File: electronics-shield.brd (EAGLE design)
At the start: 64.9 x 56 mm, 92 parts, among them IC1 TLE9201SG, IC2 TLE9201SG, IC3 TLE9201SG, IC4 TLE9201SG, IC5 AOZ1232QI-01, IC6 AOZ1232QI-01, IC7 DS3231SN#, J1 USB-MICRO-B, Q2 ON-SEMICONDUCTOR---NTZD3154NT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, Q3 ON-SEMICONDUCTOR---NTZD3154NT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, U1 STM32F0XX8T, U2 EEPROM-I2C, X1 CONNECTOR_PHOENIX_3.81, X2 Listwa zaciskowa rozłączalna 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, Y2 8MHz

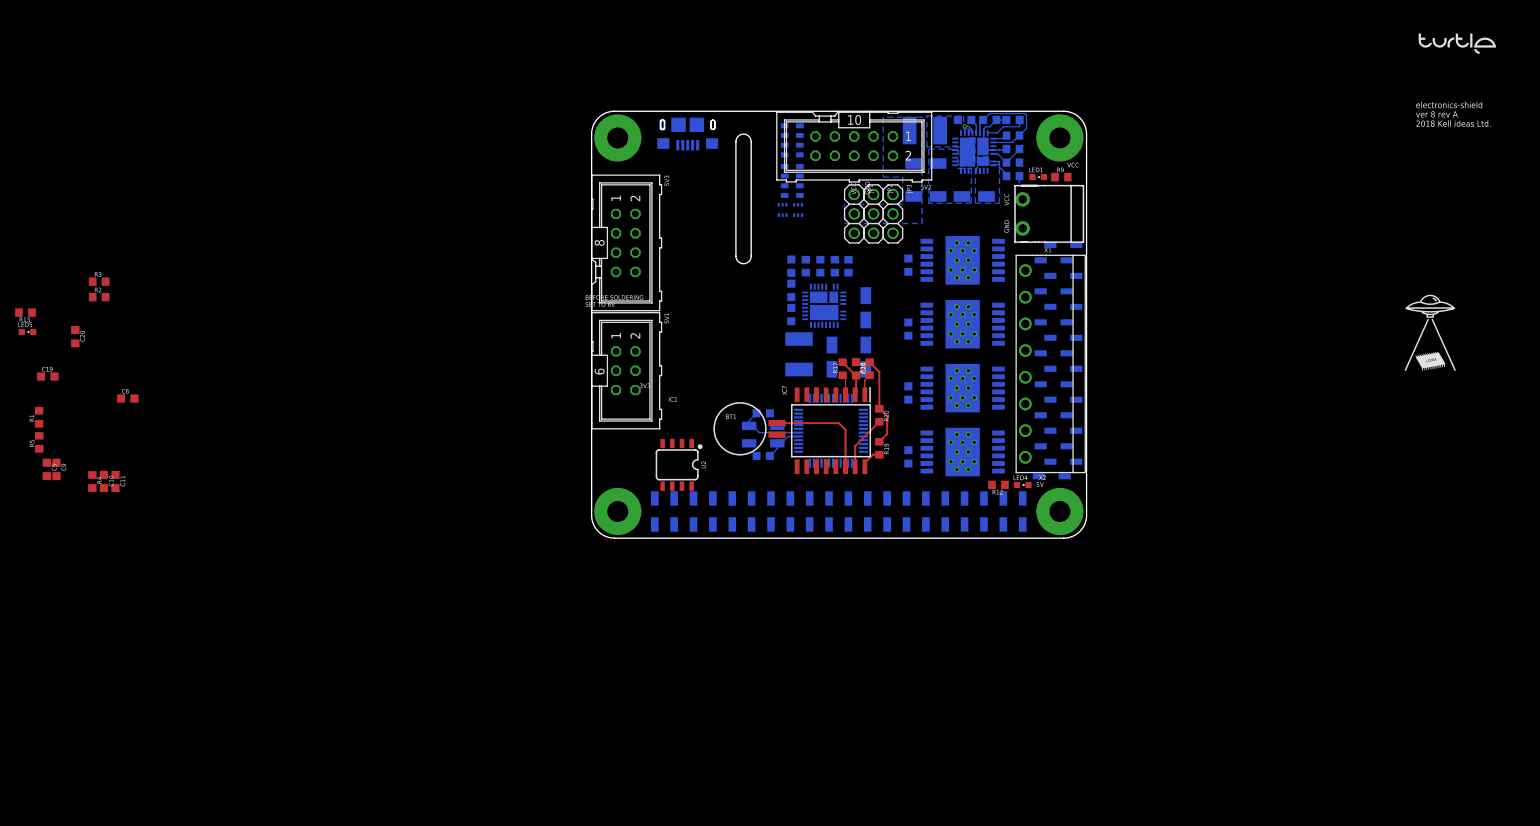
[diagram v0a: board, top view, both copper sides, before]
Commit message: Merge branch 'add_RTC' into development
First, basic layout
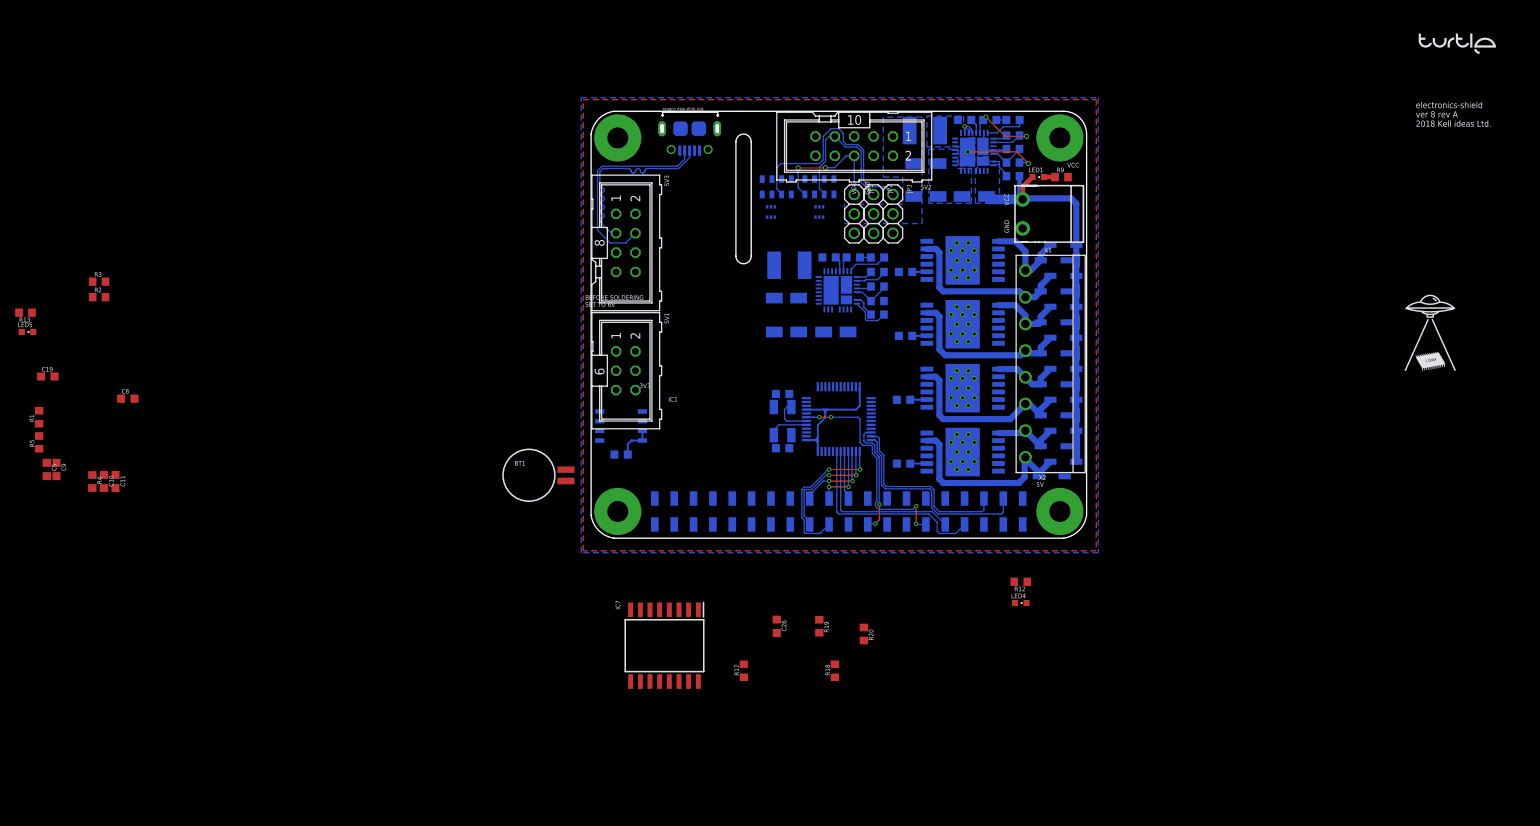
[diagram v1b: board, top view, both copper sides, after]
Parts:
- removed J1: USB-MICRO-B, Kell Ideas:USB-MICRO-B
- added USB1: ZX62-B-5PA, Seeed-Connector:MICRO-USB5+6P-SMD-0.65-AB
- moved C20 73.3 mm to (3.71, 11.1), flipped to the bottom, turned to 0 degrees
- moved R17 41.7 mm to (19.8, -17.3)
- moved R18 39.9 mm to (31.8, -17.3)
- moved IC7 35.7 mm to (9.40, -14.0)
- moved C26 35.4 mm to (24.1, -11.4)
- moved R20 28.8 mm to (35.6, -12.4)
- moved BT1 28.3 mm to (-8.38, 8.38)
- moved R19 24.7 mm to (29.7, -11.4)
- moved LED4 15.5 mm to (56.1, -8.38)
- moved R12 13.0 mm to (56.1, -5.59)
- moved L2 11.8 mm to (25.8, 35.9), turned to 0 degrees
- moved C24 11.4 mm to (37.3, 37.0), turned to 180 degrees
- moved C21 10.9 mm to (25.4, 27.2), turned to 0 degrees
- moved C22 9.78 mm to (25.4, 31.6), turned to 0 degrees
- moved R15 9.43 mm to (37.3, 35.1), turned to 0 degrees
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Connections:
- net DATA_N: now also USB1.3; no longer J1.D-
- net DATA_P: now also USB1.2; no longer J1.D+
- net GND: now also USB1.5, USB1.P1, USB1.P2, USB1.P3, USB1.P4, USB1.P5, USB1.P6; no longer J1.GND, J1.SHIELD$1, J1.SHIELD$2, J1.SHIELD$3, J1.SHIELD$4
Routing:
- net VCC: track 0.93 -> 58.6 mm
- net SERVO3: track 0.00 -> 29.8 mm
- net NRST: track 0.00 -> 29.5 mm, vias 0 -> 4
- net DATA_P: track 0.00 -> 27.2 mm
- net RPI_TXD: track 0.00 -> 27.0 mm
- net MOT41: track 0.00 -> 26.5 mm
- net DATA_N: track 0.00 -> 26.2 mm
- net MOT31: track 0.00 -> 23.9 mm
- net MOT11: track 0.00 -> 23.1 mm
- net MOT21: track 0.00 -> 22.7 mm
- net RPI_RXD: track 0.00 -> 22.2 mm
- net SCL: track 2.86 -> 24.9 mm
- net SWCLK: track 0.00 -> 20.7 mm, vias 0 -> 2
- net SDA: track 7.21 -> 27.5 mm
- net SERVO2: track 0.00 -> 19.8 mm
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- added copper zone on layer 1, net GND
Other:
- board size 64.9 x 56 mm -> 65 x 56 mm

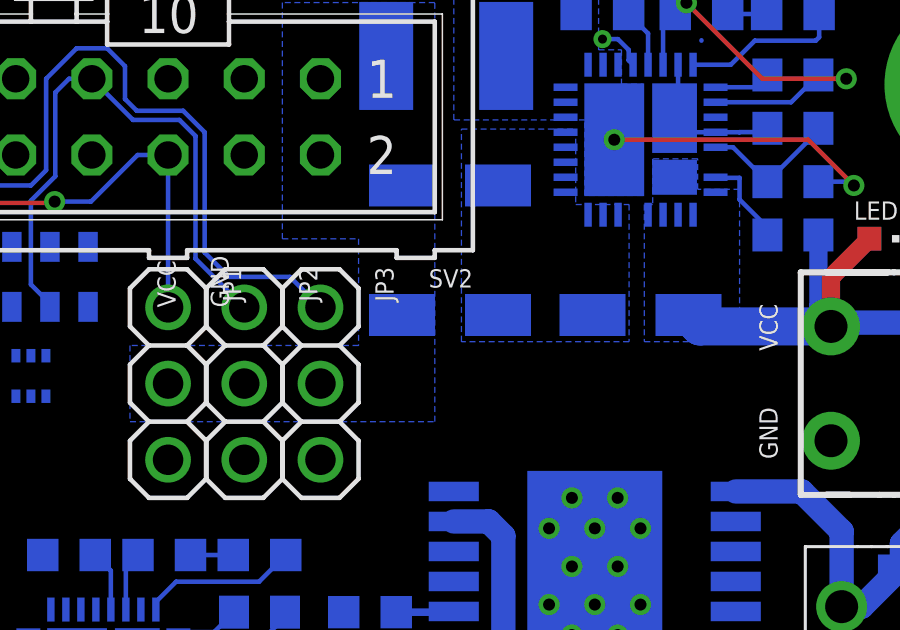
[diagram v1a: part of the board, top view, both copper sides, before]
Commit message: Added values for parts in dc-dc converter
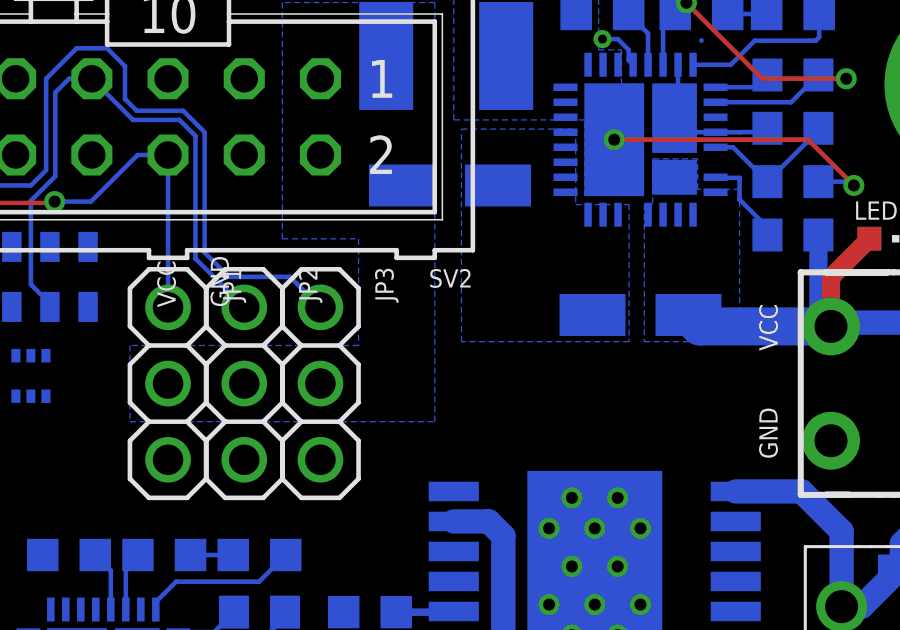
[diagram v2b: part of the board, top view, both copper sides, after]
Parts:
- removed C13: (no value), rcl:PANASONIC_B
- C12: value (none) -> 22uF
- C14: value (none) -> 100uF
- C15: value (none) -> 100n
- C16: value (none) -> 1uf
- C17: value (none) -> 1nF
- L1, L2: value (none) -> 100uH
- R6: value (none) -> 65k
- R7: value (none) -> 10k
- R8: value (none) -> 100k
- renumbered R10 to 456
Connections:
- net GND: no longer C13.-
- net VCC_SERVO: no longer C13.+

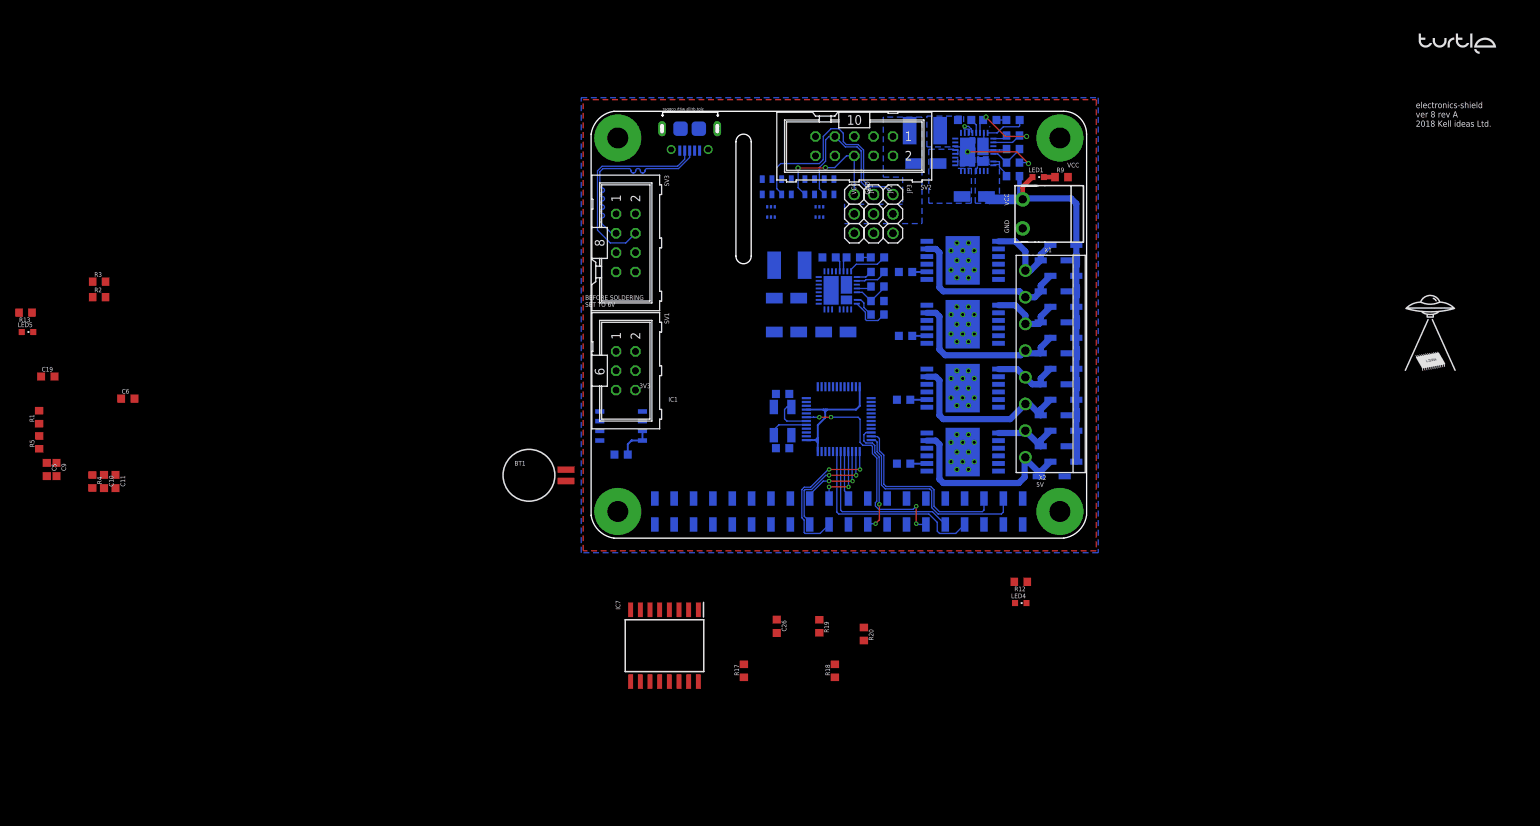
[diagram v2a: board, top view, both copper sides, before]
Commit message: Minor changes, changed RTC, added 3V3 regulator, changed USB connector, added fuses, reverse polarity protection, changed footprint for Schottky diodes, added filtering to input voltage, change in layout
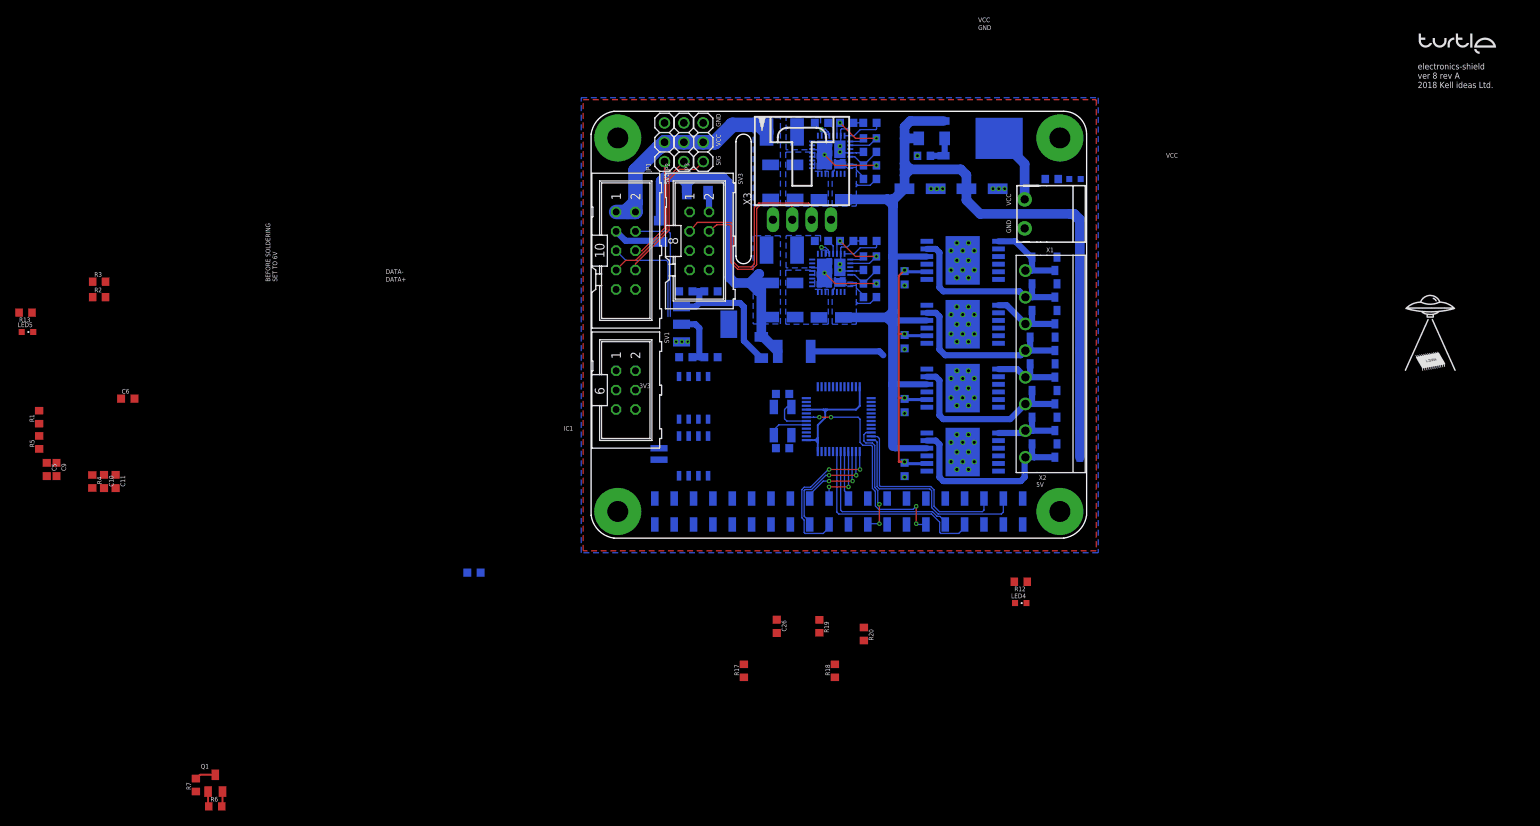
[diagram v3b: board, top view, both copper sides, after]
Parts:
- removed 456: (no value), Kell Ideas:R0603
- removed C19: (no value), Kell Ideas:C0603K
- removed IC5: AOZ1232QI-01, Kell Ideas:AOZ1232QI01
- removed IC7: DS3231SN#, Kell Ideas:SOIC127P1032X265-16N
- removed L1: 100uH, rcl:L4532P
- removed Q3: ON-SEMICONDUCTOR---NTZD3154NT1G_ON_SEMICONDUCTOR_NTZD3154NT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, electronics-shield:ON-SEMICONDUCTOR---NTZD3154NT1G_ON_SEMICONDUCTOR_NTZD3154NT1G_0
- removed RN1, RN2: 1k, SparkFun-Resistors:0805-ARV
- removed USB1: ZX62-B-5PA, Seeed-Connector:MICRO-USB5+6P-SMD-0.65-AB
- added C13: 47uF, rcl:PANASONIC_C
- added C27, C31, C32: 33uF/10V, rcl:PANASONIC_B
- added C28: 100n, Kell Ideas:C0603K
- added C29: 1nF, Kell Ideas:C0603K
- added C30: 1uF/35V, Kell Ideas:C0603K
- added D17: 10V, diode:SOD80C
- added F1, F2, F5: 750mA, Seeed-Fuse:F1206
- added F3: MF-MSMF050-2, Seeed-Fuse:F1812
- added IC8: AOZ1232QI-01, Kell Ideas:AOZ1232QI01
- added L3: 1uH, rcl:L4532P
- added Q1: (no value), adafruit:SOT23
- added R21: 10k, Kell Ideas:R0603
- added R22: 100k, Kell Ideas:R0603
- added R23, R24: 456, Kell Ideas:R0603
- added U3: MAXIM_DS3231MZ+MAXIM_DS3231MZ+_0_0, Kell Ideas:MAXIM_DS3231MZ+_0
- added U4: V_REG_317SMD, Kell Ideas:SOT223
- added X3: C-GRID-04-70553, con-molex:70553-04
- C1, C2, C3, C4: value (none) -> 100nF
- C12: value 22uF -> 47uF; device rcl:PANASONIC_B -> rcl:PANASONIC_C
- C14: value 100uF -> 22uF; device rcl:PANASONIC_B -> Kell Ideas:C0603K
- C15: value 100n -> 100nF
- C16: value 1uf -> 100nF
- C17: value 1nF -> 22uF
- C18: value (none) -> 22uF/35V
- C21: value (none) -> 33uF/10V
- C22: value (none) -> 100n; device rcl:PANASONIC_B -> Kell Ideas:C0603K
- C23: value (none) -> 1nF
- C24: value (none) -> 1uF/35V
- C25: value (none) -> 22uF/35V; device Kell Ideas:C0603K -> rcl:PANASONIC_B
- D1, D10, D11, D12, D13, D14, D15, D16, D2, D3, D4, D5, D6, D7, D8, D9: value SK38SMA -> 80V/3A; device Kell Ideas:SOD123 -> adafruit:SOD-123FL
- L2: value 100uH -> 1uH
- Q2: value ON-SEMICONDUCTOR---NTZD3154NT1G_ON_SEMICONDUCTOR_NTZD3154NT1GON_SEMICONDUCTOR_NTZD3154NT1G_0_0 -> IRFR5305; device electronics-shield:ON-SEMICONDUCTOR---NTZD3154NT1G_ON_SEMICONDUCTOR_NTZD3154NT1G_0 -> transistor-power:D-PAK_TO252AA
- R11, R16: value (none) -> 65k
- R14: value (none) -> 10k
- R15: value (none) -> 100k
- R6: value 65k -> 10k; device Kell Ideas:R0603 -> rcl:R0603
- R7: device Kell Ideas:R0603 -> rcl:R0603
- R8: value 100k -> 10k; device Kell Ideas:R0603 -> rcl:R0603
- moved R7 135.8 mm to (-52.1, -32.3), flipped to the top, turned to 90 degrees
- moved R6 134.5 mm to (-49.5, -35.1), flipped to the top
- moved C17 50.4 mm to (15.5, 23.9), turned to 0 degrees
- moved C15 42.9 mm to (12.2, 32.5)
- moved C16 42.9 mm to (15.5, 32.5)
- moved C14 40.5 mm to (12.2, 23.9), turned to 180 degrees
- moved SV2 33.0 mm to (4.32, 37.8), turned to 270 degrees
- moved Q2 29.1 mm to (50.8, 52.6)
- moved JP1 26.6 mm to (9.40, 52.1), turned to 90 degrees
- moved JP2 26.6 mm to (11.9, 52.1), turned to 90 degrees
- moved JP3 26.6 mm to (14.5, 52.1), turned to 90 degrees
- moved C20 24.8 mm to (-15.6, -4.39)
- moved C22 23.4 mm to (30.0, 54.6), turned to 180 degrees
- moved C21 21.9 mm to (24.9, 49.1)
- moved C23 18.5 mm to (36.3, 54.6)
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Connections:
- removed net +5V/2: SV2.3
- removed net BST: C15.2, IC5.27
- removed net FB: IC5.5, R6.2, R7.1
- removed net LX: C15.1, IC5.20, IC5.21, IC5.22, IC5.23, IC5.24, IC5.25, IC5.31, L1.1, R6.1
- removed net LX1: C23.1, IC6.20, IC6.21, IC6.22, IC6.23, IC6.24, IC6.25, IC6.31, L2.1, R11.1
- removed net N$14: Q2.4, RN2.3
- removed net N$16: Q2.3, RN2.4
- removed net PGOOD: IC5.1, R8.2
- removed net SEN1: U1.10
- removed net SEN2: U1.11
- removed net SEN3: U1.12
- removed net SEN4: U1.13
- removed net SS: C17.2, IC5.30
- removed net TON: 456.2, IC5.6
- removed net VCC_INT: C16.2, IC5.2, IC5.28, R8.1
- new net BST2: C28.2, IC8.27
- new net FB2: IC8.5, R16.2, R21.1
- new net LX2: C28.1, IC8.20, IC8.21, IC8.22, IC8.23, IC8.24, IC8.25, IC8.31, L3.1, R16.1
- new net LX3: C22.1, IC6.20, IC6.21, IC6.22, IC6.23, IC6.24, IC6.25, IC6.31, L2.1, R11.1
- new net N$12: F2.2, SV2.3
- new net N$13: D17.A, Q2.1, R8.2
- new net N$15: F1.1, SV3.2
- new net N$17: C15.2, C16.2, F5.2, U4.3
- new net N$18: F3.1, PCB1.2, PCB1.4
- new net PGOOD2: IC8.1, R22.2
- new net SS2: C29.2, IC8.30
- new net TON2: IC8.6, R23.2
- new net UART_SELECTOR: PCB1.7
- new net V+: Q2.4, X1.2
- new net VBAT: U3.6
- new net VCC_INT2: C30.2, IC8.2, IC8.28, R22.1
- net +3V3: now also C14.2, C17.2, Q1.1, R6.1, U4.2; no longer IC7.2, Q2.2, Q2.5, Q3.2, Q3.5, RN1.6, RN1.8, RN2.6, RN2.8
- net +5V: now also C27.+, C31.+, F1.2, F2.1, F3.2, F5.1, L3.2, R7.1; no longer C19.1, C21.+, C22.+, L2.2, PCB1.2, PCB1.4, RN1.5, RN1.7, RN2.5, RN2.7, SV3.2
- net BATTERY: no longer IC7.14
- net BST1: now also C22.2; no longer C23.2
- net DATA_N: now also X3.3; no longer USB1.3
- net DATA_P: now also X3.2; no longer USB1.2
- net GND: now also C13.-, C14.1, C15.1, C23.1, C25.-, C27.-, C29.1, C30.1, C31.-, C32.-, D10.A, D11.A, D12.A, D13.A, D14.A, D15.A, D16.A, D9.A, IC8.12, IC8.13, IC8.14, IC8.15, IC8.16, IC8.17, IC8.18, IC8.19, IC8.26, IC8.29, IC8.32, IC8.4, R21.2, R8.1, U3.5, U4.1, X3.1; no longer C14.-, C19.2, C22.-, C25.1, D10.2, D11.2, D12.2, D13.2, D14.2, D15.2, D16.2, D9.2, IC5.12, IC5.13, IC5.14, IC5.15, IC5.16, IC5.17, IC5.18, IC5.19, IC5.26, IC5.29, IC5.32, IC5.4, IC7.10, IC7.11, IC7.12, IC7.13, IC7.4, IC7.5, IC7.6, IC7.7, IC7.8, IC7.9, R7.2, USB1.5, USB1.P1, USB1.P2, USB1.P3, USB1.P4, USB1.P5, USB1.P6
- net MOT11: now also D16.C, D8.A; no longer D16.1, D8.2
- net MOT12: now also D15.C, D7.A; no longer D15.1, D7.2
- net MOT21: now also D14.C, D6.A; no longer D14.1, D6.2
- net MOT22: now also D13.C, D5.A; no longer D13.1, D5.2
- net MOT31: now also D12.C, D4.A; no longer D12.1, D4.2
- net MOT32: now also D11.C, D3.A; no longer D11.1, D3.2
- net MOT41: now also D10.C, D2.A; no longer D10.1, D2.2
- net MOT42: now also D1.A, D9.C; no longer D1.2, D9.1
- net N$2: no longer IC7.1
- net N$3: no longer IC7.3
- net SCL: no longer IC7.16
- net SDA: no longer IC7.15
- net SERVO1: no longer Q3.3, RN1.4
- net SERVO1_UC: no longer Q3.4, RN1.3
- net SERVO2: now also Q1.3, R7.2; no longer Q3.6, RN1.2
- net SERVO2_UC: now also Q1.2, R6.2; no longer Q3.1, RN1.1
- net SERVO3: no longer Q2.6, RN2.2
- net SERVO3_UC: no longer Q2.1, RN2.1
- net SS1: now also C23.2; no longer C24.2
- net TON1: now also R24.2; no longer R16.2
- net VCC: now also C13.+, C25.+, D1.C, D17.C, D2.C, D3.C, D4.C, D5.C, D6.C, D7.C, D8.C, IC8.10, IC8.11, IC8.33, IC8.7, IC8.8, IC8.9, Q2.3, R23.1, R24.1, U3.2; no longer 456.1, D1.1, D2.1, D3.1, D4.1, D5.1, D6.1, D7.1, D8.1, IC5.10, IC5.11, IC5.33, IC5.7, IC5.8, IC5.9, R16.1, X1.2
- net VCC_INT1: now also C24.2; no longer C25.2
- net VCC_SERVO: now also C21.+, C32.+, L2.2; no longer C14.+, L1.2
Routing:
- net VCC: track 58.6 -> 152.1 mm
- net +5V: track 0.00 -> 52.3 mm
- net +3V3: track 32.4 -> 69.9 mm, vias 0 -> 4
- net VCC_SERVO: track 0.00 -> 35.2 mm
- net N$17: track 0.00 -> 19.3 mm
- net SDA_RX: track 0.00 -> 15.6 mm
- net SCL_TX: track 0.00 -> 14.6 mm
- net VCC_INT: track 13.5 -> 0.00 mm, vias 2 -> 0
- net GND: track 11.5 -> 23.3 mm, vias 49 -> 68
- net VCC_INT2: track 0.00 -> 11.3 mm, vias 0 -> 2
- net SERVO3: track 29.8 -> 19.1 mm
- net LX: track 9.85 -> 0.00 mm, vias 2 -> 0
- net N$18: track 0.00 -> 9.74 mm
- net V+: track 0.00 -> 9.39 mm
- net LX2: track 0.00 -> 7.38 mm, vias 0 -> 2
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- added copper zone on layer 16, net +5V
- added copper zone on layer 16, net LX2
- added copper zone on layer 16, net LX3
- removed copper zone on layer 16, net LX
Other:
- board text added: "+6V"
- board text added: "750mA"
- board text removed: "+7V/1"
- board text removed: "+7V/2"
